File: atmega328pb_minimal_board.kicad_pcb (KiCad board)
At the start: 2 copper layers, 54 x 33.7 mm, 14 parts, among them J1 Conn_01x02_Male, J2 Conn_02x05_Odd_Even, J3 Conn_01x16_Male, J4 Conn_01x16_Male, J5 Conn_01x02_Male, U1 ATmega328PB-AU, Y1 16MHz

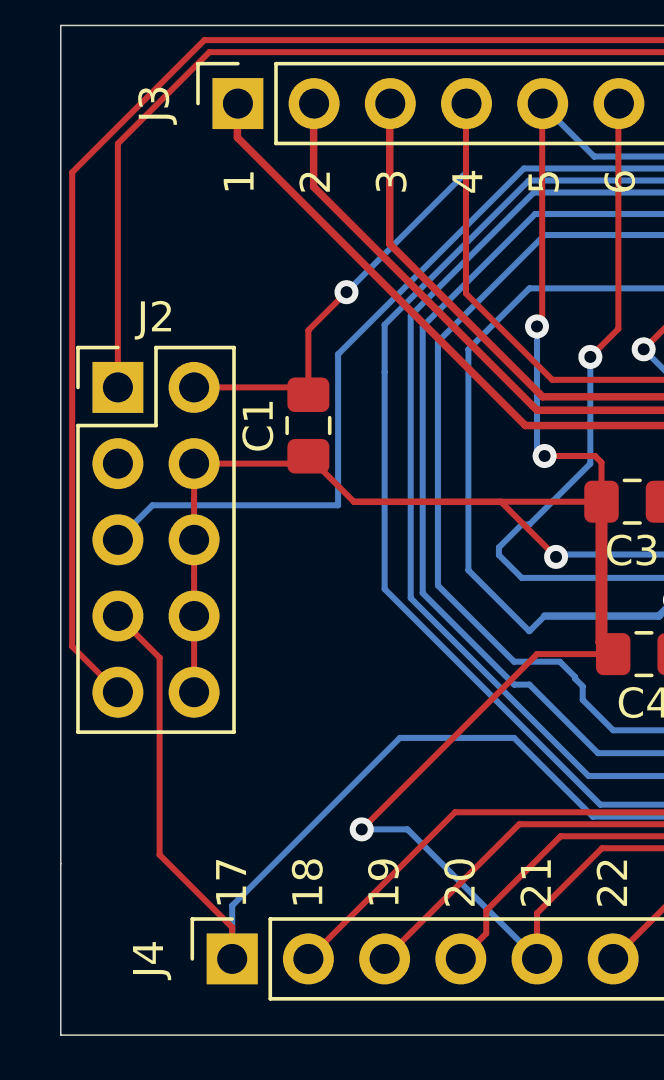
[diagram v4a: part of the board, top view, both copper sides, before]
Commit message: update front silkscreen around the ICSP. Update docs.
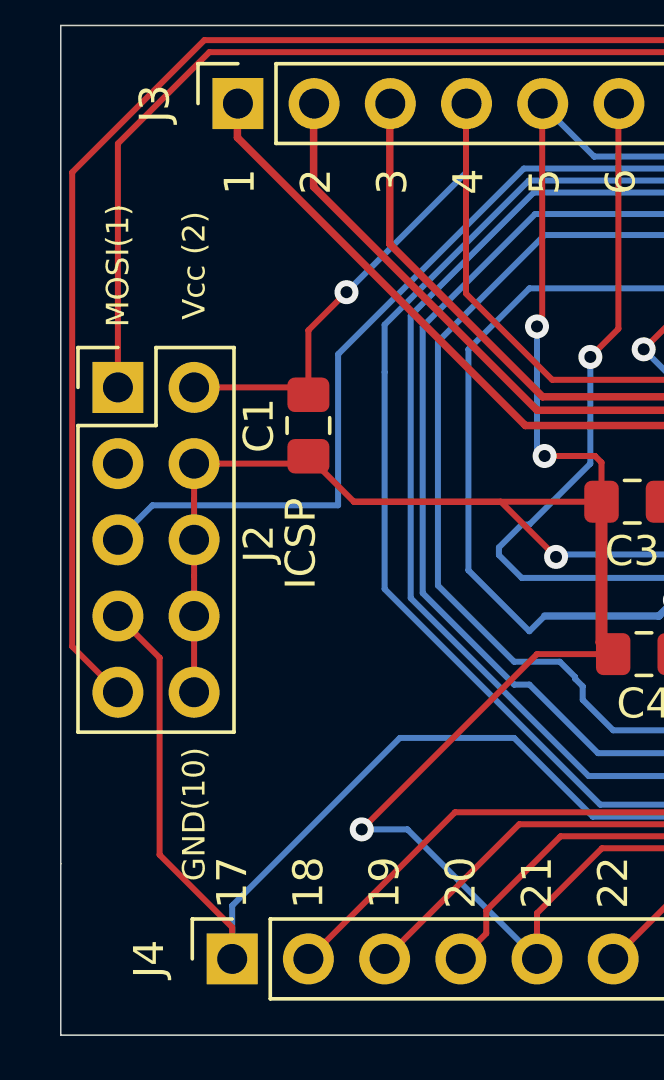
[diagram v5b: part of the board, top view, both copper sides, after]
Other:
- board text added: "GND(10)"
- board text added: "ICSP"
- board text added: "MOSI(1)"
- board text added: "Vcc (2)"
